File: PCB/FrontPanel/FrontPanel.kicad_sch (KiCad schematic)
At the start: 51 parts, among them J1 Conn_01x05, J2 SWD, Q3 2N7002, SW1 RotaryEncoder_Switch, SW2 IndepChSelect, SW3 SeriesChSelect, SW4 ParChSelect, SW5 ChAEnable, SW6 ChBEnable, SW7 ABSelect, SW8 LArrow, SW9 RArrow, U1 MCU_ST_STM32G0:STM32G031F6Px, U2 CD74HC4067SM

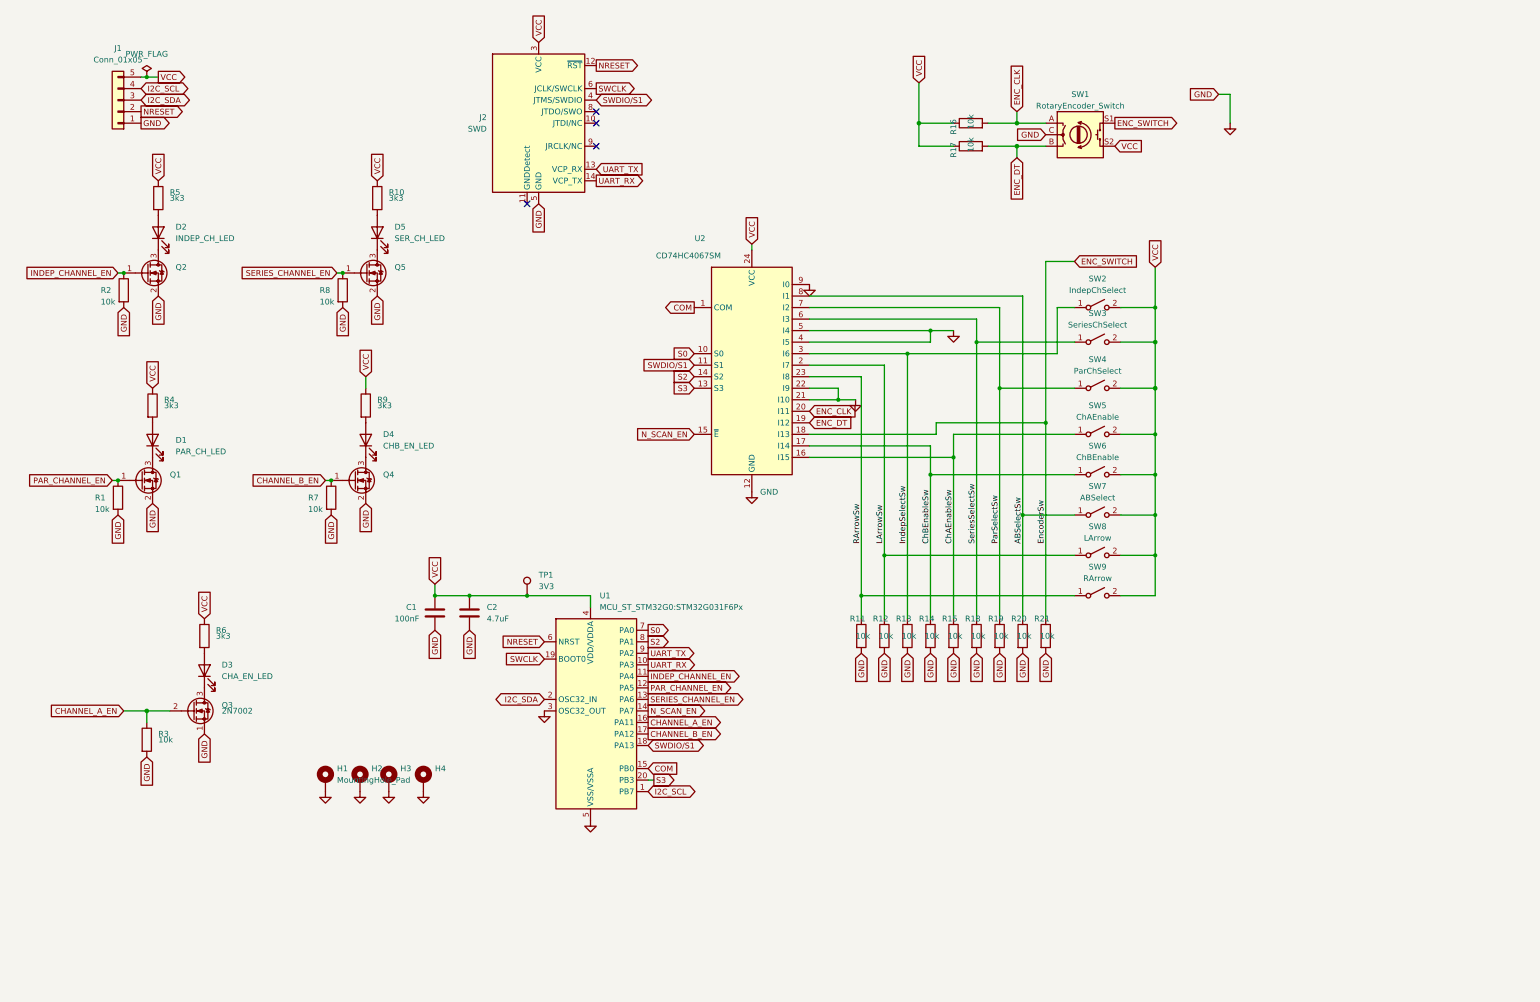
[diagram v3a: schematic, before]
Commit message: Fixes for the front panel
Add a 3V3 regulator to convert the 5V input.
Fix RX/TX mix-up
Fix footprint for one last 2N7002 mosfet
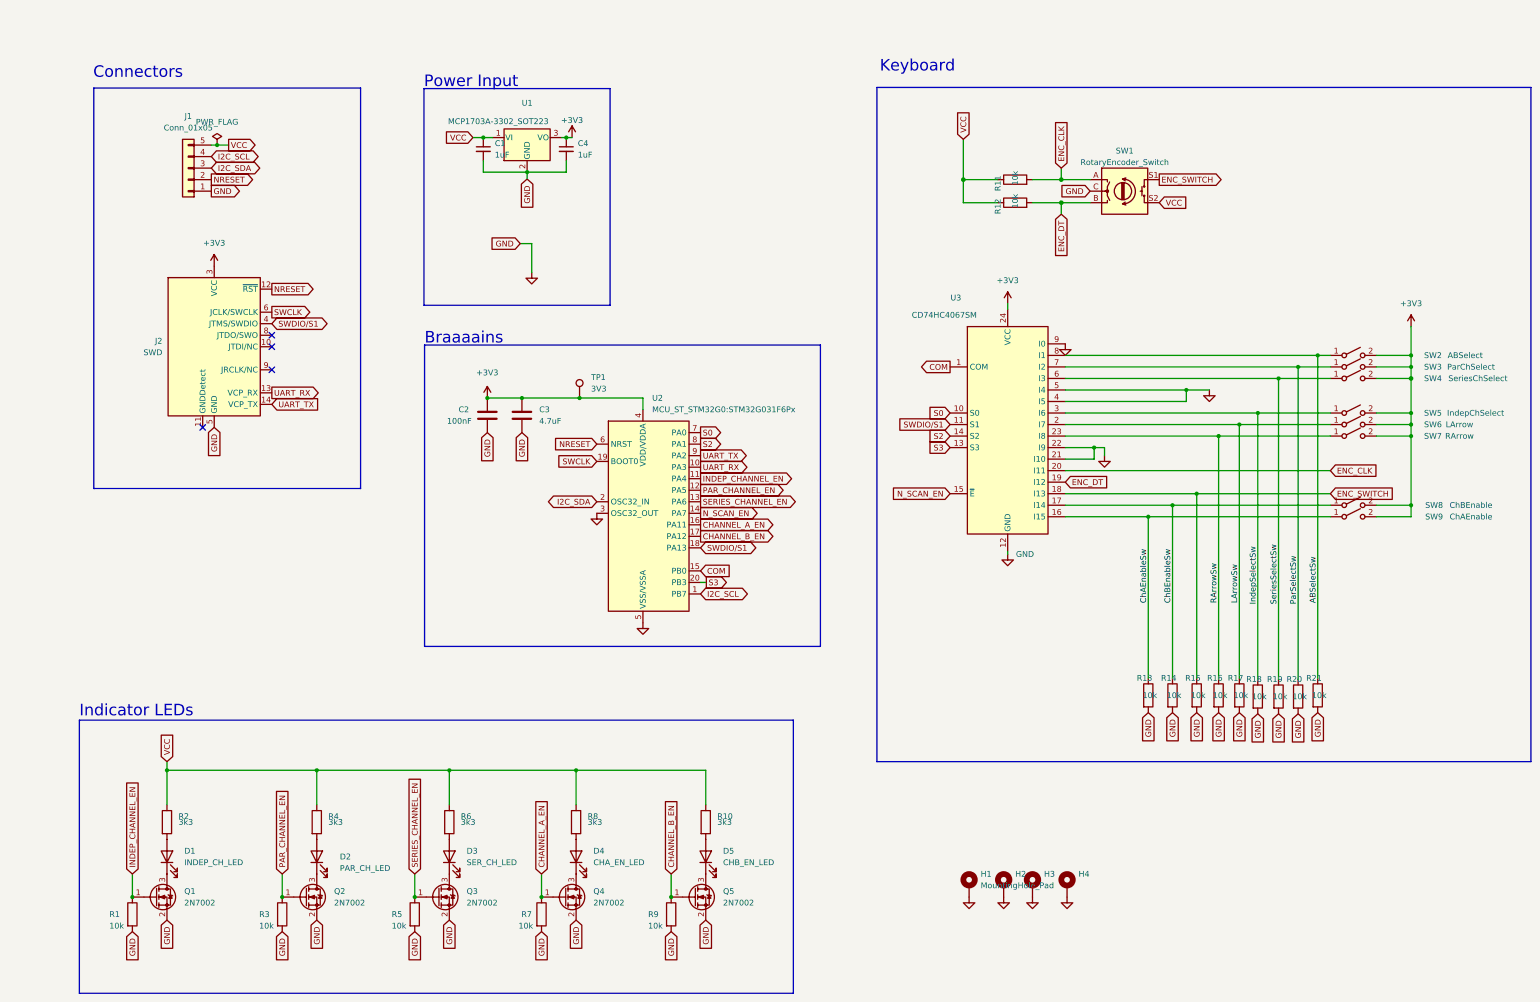
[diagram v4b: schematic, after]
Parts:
- removed Q3: 2N7002, Package_TO_SOT_SMD:SOT-23, symbol Transistor_FET:2N7000
- added C1, C4: 1uF, Capacitor_SMD:C_0805_2012Metric, symbol Device:C_Small
- added Q4: 2N7002, Package_TO_SOT_SMD:SOT-23, symbol Transistor_FET:2N7002
- added U1: MCP1703A-3302_SOT223, Package_TO_SOT_SMD:SOT-223-3_TabPin2, symbol Regulator_Linear:MCP1703A-3302_SOT223
- Q1: renamed from Q2; value (none) -> 2N7002; footprint (none) -> Package_TO_SOT_SMD:SOT-23
- Q2: renamed from Q1; value (none) -> 2N7002; footprint (none) -> Package_TO_SOT_SMD:SOT-23
- Q3: renamed from Q5; value (none) -> 2N7002; footprint (none) -> Package_TO_SOT_SMD:SOT-23
- Q5: renamed from Q4; value (none) -> 2N7002; footprint (none) -> Package_TO_SOT_SMD:SOT-23
- renumbered C1 to C2, C2 to C3, D2 to D1, D1 to D2, D5 to D3, D3 to D4, D4 to D5, R2 to R1, R9 to R10, R16 to R11, R17 to R12, R15 to R13, R21 to R15, R11 to R16, R12 to R17, R13 to R18, R18 to R19, R5 to R2, R19 to R20, R20 to R21, R1 to R3, R8 to R5, R10 to R6, R3 to R7, R6 to R8, R7 to R9, SW7 to SW2, SW4 to SW3, SW3 to SW4, SW2 to SW5, SW8 to SW6, SW9 to SW7, SW6 to SW8, SW5 to SW9, U1 to U2, U2 to U3
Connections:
- net CHANNEL_A_EN: now also Q4.1 (G)
- net GND: now also C1.2, C4.2, Q4.2 (S), U1.2 (GND)
- net UART_RX: now also J2.13 (VCP_RX); no longer J2.14 (VCP_TX)
- net UART_TX: now also J2.14 (VCP_TX); no longer J2.13 (VCP_RX)
- net VCC: now also C1.1, U1.1 (VI); no longer C2.1, C3.1, J2.3 (VCC), SW2.2 (B), SW3.2 (B), SW4.2 (B), SW5.2 (B), SW6.2 (B), SW7.2 (B), SW8.2 (B), SW9.2 (B), TP1.1, U2.4 (VDD/VDDA), U3.24 (VCC)
- net at D4.1 (K): now also Q4.3 (D)
- new net +3V3: C2.1, C3.1, C4.1, J2.3 (VCC), SW2.2 (B), SW3.2 (B), SW4.2 (B), SW5.2 (B), SW6.2 (B), SW7.2 (B), SW8.2 (B), SW9.2 (B), TP1.1, U1.3 (VO), U2.4 (VDD/VDDA), U3.24 (VCC)
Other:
- note added: "Braaaains"
- note added: "Connectors"
- note added: "Indicator LEDs"
- note added: "Keyboard"
- note added: "Power Input"
- moved on the sheet: C2, C3, D1, D2, D3, D4, D5, H1, H2, H3, H4, J1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
